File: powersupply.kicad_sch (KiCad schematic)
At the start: 25 parts, among them J1 5V In, J2 Vdrive In, U1 AP63203WU, U2 AP2112K-3.3

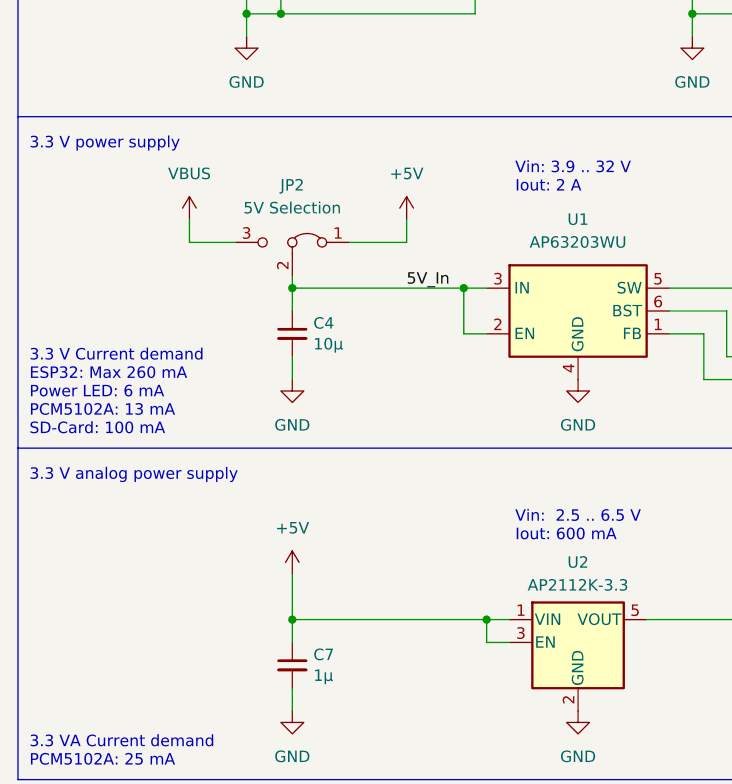
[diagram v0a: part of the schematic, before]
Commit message: - I2C entfernt - Logo hinzugefügt - Spannungsauswahl für Audio (USB oder +5V) hinzugefügt - Spannung für WS2812 LEDs ändert sich jetzt zusammen mit +5VD Auswahl
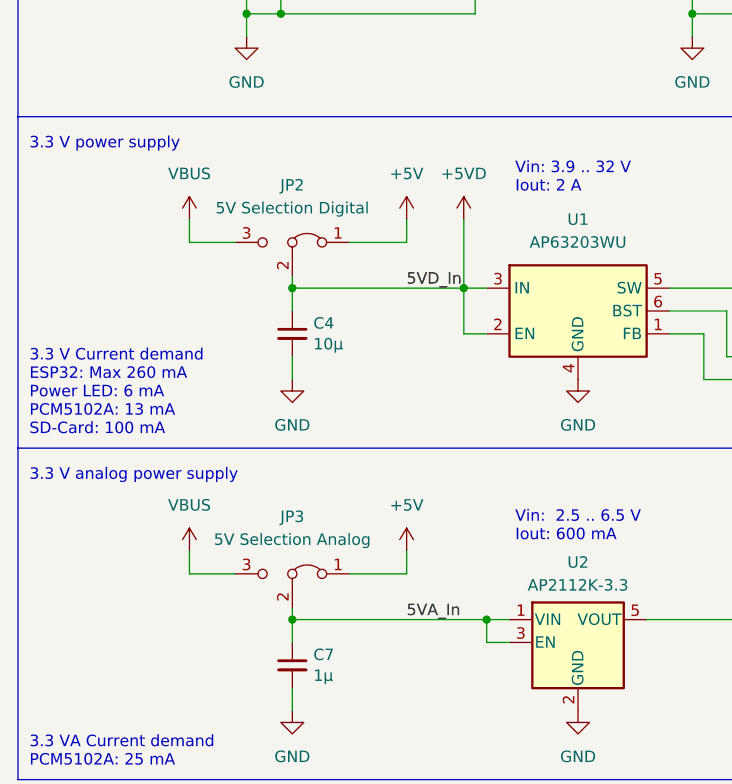
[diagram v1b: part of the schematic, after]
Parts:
- added JP3: 5V Selection Analog, Connector_PinHeader_2.54mm:PinHeader_1x03_P2.54mm_Vertical, symbol Jumper:Jumper_3_Bridged12
- JP2: value 5V Selection -> 5V Selection Digital
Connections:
- net +5V: now also JP3.1 (A); no longer C7.1, U2.1 (VIN), U2.3 (EN)
- net VBUS: now also JP3.3 (B)
- net 5V_In renamed +5VD
- new net 5VA_In: C7.1, JP3.2 (C), U2.1 (VIN), U2.3 (EN)

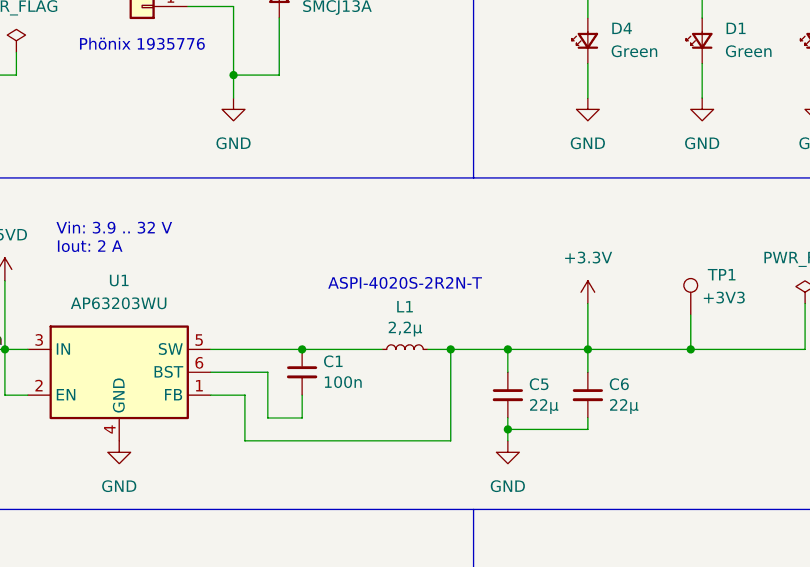
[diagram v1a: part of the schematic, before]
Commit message: Footprint changes
Changed WS2812 from 5050 to 2020
Changed ESP32 to correct revision
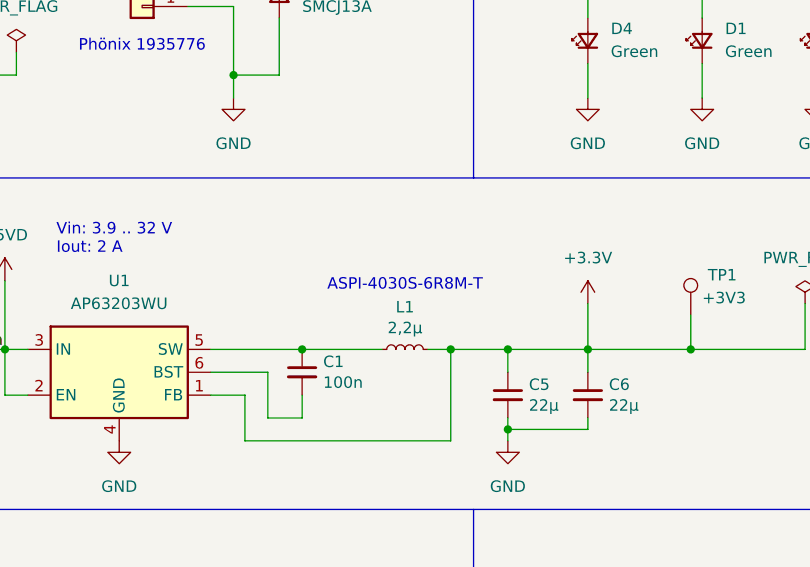
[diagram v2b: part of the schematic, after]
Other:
- note added: "ASPI-4030S-6R8M-T"
- note removed: "ASPI-4020S-2R2N-T"
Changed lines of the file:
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@@
 		)
 	)
-	(text "ASPI-4020S-2R2N-T"
+	(text "ASPI-4030S-6R8M-T"
 		(exclude_from_sim no)
 		(at 119.38 81.28 0)

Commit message: First Manufactured Version
A few silkscreen changes
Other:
- moved on the sheet: C1, U1
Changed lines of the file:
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@@
 	(text "Vin:  2.5 .. 6.5 V\nIout: 600 mA"
 		(exclude_from_sim no)
-		(at 80.645 112.395 0)
+		(at 85.344 110.236 0)
 		(effects
 			(font
@@
 	(text "Vin: 3.9 .. 32 V\nIout: 2 A"
 		(exclude_from_sim no)
-		(at 80.645 73.66 0)
+		(at 84.455 73.66 0)
 		(effects
 			(font
@@
 	)
 	(junction
+		(at 74.93 92.71)
+		(diameter 0)
+		(color 0 0 0 0)
+	)
+	(junction
 		(at 74.93 87.63)
 		(diameter 0)
@@
 	)
 	(junction
-		(at 107.95 87.63)
+		(at 111.76 87.63)
 		(diameter 0)
 		(color 0 0 0 0)
@@
 	(wire
 		(pts
-			(xy 97.79 87.63) (xy 107.95 87.63)
+			(xy 101.6 87.63) (xy 111.76 87.63)
 		)
 		(stroke
@@
 	(wire
 		(pts
-			(xy 77.47 92.71) (xy 74.93 92.71)
+			(xy 81.28 92.71) (xy 74.93 92.71)
 		)
 		(stroke
@@
 	(wire
 		(pts
-			(xy 97.79 92.71) (xy 101.6 92.71)
+			(xy 101.6 92.71) (xy 105.41 92.71)
 		)
 		(stroke
@@
 	(wire
 		(pts
-			(xy 97.79 90.17) (xy 104.14 90.17)
+			(xy 101.6 90.17) (xy 107.95 90.17)
 		)
 		(stroke
@@
 	(wire
 		(pts
-			(xy 107.95 95.25) (xy 107.95 92.71)
+			(xy 111.76 95.25) (xy 111.76 92.71)
 		)
 		(stroke
@@
 	(wire
 		(pts
-			(xy 104.14 90.17) (xy 104.14 95.25)
+			(xy 107.95 90.17) (xy 107.95 95.25)
 		)
 		(stroke
@@
 	(wire
 		(pts
-			(xy 74.93 87.63) (xy 77.47 87.63)
+			(xy 74.93 87.63) (xy 81.28 87.63)
 		)
 		(stroke
@@
 	(wire
 		(pts
-			(xy 104.14 95.25) (xy 107.95 95.25)
+			(xy 107.95 95.25) (xy 111.76 95.25)
 		)
 		(stroke
@@
 	(wire
 		(pts
+			(xy 77.47 119.38) (xy 77.47 124.46)
+		)
+		(stroke
+			(width 0)
+			(type default)
+		)
+	)
+	(wire
+		(pts
 			(xy 55.88 124.46) (xy 55.88 123.19)
 		)
@@
 	(wire
 		(pts
-			(xy 101.6 92.71) (xy 101.6 97.79)
+			(xy 105.41 92.71) (xy 105.41 97.79)
 		)
 		(stroke
@@
 	(wire
 		(pts
-			(xy 107.95 87.63) (xy 116.84 87.63)
+			(xy 111.76 87.63) (xy 116.84 87.63)
 		)
 		(stroke
@@
 	(wire
 		(pts
-			(xy 101.6 97.79) (xy 124.46 97.79)
+			(xy 105.41 97.79) (xy 124.46 97.79)
 		)
 		(stroke
@@
 		)
 	)
-	(label "5VD_In"
-		(at 68.58 87.63 0)
+	(label "+5VD"
+		(at 67.31 87.63 0)
 		(effects
 			(font
@@
 	(symbol
 		(lib_id "Device:C_Small")
-		(at 107.95 90.17 0)
+		(at 111.76 90.17 0)
 		(unit 1)
 		(exclude_from_sim no)
@@
 		(dnp no)
 		(property "Reference" "C1"
-			(at 110.2868 89.0016 0)
+			(at 114.0968 89.0016 0)
 			(effects
 				(font
@@
 		)
 		(property "Value" "100n"
-			(at 110.2868 91.313 0)
+			(at 114.0968 91.313 0)
 			(effects
 				(font
@@
 		)
 		(property "Footprint" "Capacitor_SMD:C_0603_1608Metric"
-			(at 107.95 90.17 0)
+			(at 111.76 90.17 0)
 			(effects
 				(font
@@
 		)
 		(property "Datasheet" "~"
-			(at 107.95 90.17 0)
+			(at 111.76 90.17 0)
 			(effects
 				(font
@@
 		)
 		(property "Description" ""
-			(at 107.95 90.17 0)
+			(at 111.76 90.17 0)
 			(effects
 				(font
@@
 	(symbol
 		(lib_id "Regulator_Switching:AP63203WU")
-		(at 87.63 90.17 0)
+		(at 91.44 90.17 0)
 		(unit 1)
 		(exclude_from_sim no)
@@
 		(fields_autoplaced yes)
 		(property "Reference" "U1"
-			(at 87.63 80.01 0)
+			(at 91.44 80.01 0)
 			(effects
 				(font
@@
 		)
 		(property "Value" "AP63203WU"
-			(at 87.63 82.55 0)
+			(at 91.44 82.55 0)
 			(effects
 				(font
@@
 		)
 		(property "Footprint" "Package_TO_SOT_SMD:TSOT-23-6"
-			(at 87.63 113.03 0)
+			(at 91.44 113.03 0)
 			(effects
 				(font
@@
 		)
 		(property "Datasheet" "https://www.diodes.com/assets/Datasheets/AP63200-AP63201-AP63203-AP63205.pdf"
-			(at 87.63 90.17 0)
+			(at 91.44 90.17 0)
 			(effects
 				(font
@@
 		)
 		(property "Description" ""
-			(at 87.63 90.17 0)
+			(at 91.44 90.17 0)
 			(effects
 				(font
@@
 	)
 	(symbol
+		(lib_id "power:PWR_FLAG")
+		(at 77.47 119.38 0)
+		(mirror y)
+		(unit 1)
+		(exclude_from_sim no)
+		(in_bom yes)
+		(on_board yes)
+		(dnp no)
+		(property "Reference" "#FLG08"
+			(at 77.47 117.475 0)
+			(effects
+				(font
+					(size 1.27 1.27)
+				)
+				(hide yes)
+			)
+		)
+		(property "Value" "PWR_FLAG"
+			(at 77.47 114.3 0)
+			(effects
+				(font
+					(size 1.27 1.27)
+				)
+			)
+		)
+		(property "Footprint" ""
+			(at 77.47 119.38 0)
+			(effects
+				(font
+					(size 1.27 1.27)
+				)
+				(hide yes)
+			)
+		)
+		(property "Datasheet" "~"
+			(at 77.47 119.38 0)
+			(effects
+				(font
+					(size 1.27 1.27)
+				)
+				(hide yes)
+			)
+		)
+		(property "Description" "Special symbol for telling ERC where power comes from"
+			(at 77.47 119.38 0)
+			(effects
+				(font
+					(size 1.27 1.27)
+				)
+				(hide yes)
+			)
+		)
+		(pin "1"
+		)
+		(instances
+			(project "BigCore"
+				(path "/9351c569-8a22-403a-823f-92ee14b5d151/de348b60-5b93-45ac-b286-4b82c099f6e0"
+					(reference "#FLG08")
+					(unit 1)
+				)
+			)
+		)
+	)
+	(symbol
 		(lib_id "Device:C_Small")
 		(at 55.88 92.71 0)
@@
 	)
 	(symbol
+		(lib_id "power:PWR_FLAG")
+		(at 74.93 92.71 0)
+		(mirror x)
+		(unit 1)
+		(exclude_from_sim no)
+		(in_bom yes)
+		(on_board yes)
+		(dnp no)
+		(property "Reference" "#FLG07"
+			(at 74.93 94.615 0)
+			(effects
+				(font
+					(size 1.27 1.27)
+				)
+				(hide yes)
+			)
+		)
+		(property "Value" "PWR_FLAG"
+			(at 74.93 97.79 0)
+			(effects
+				(font
+					(size 1.27 1.27)
+				)
+			)
+		)
+		(property "Footprint" ""
+			(at 74.93 92.71 0)
+			(effects
+				(font
+					(size 1.27 1.27)
+				)
+				(hide yes)
+			)
+		)
+		(property "Datasheet" "~"
+			(at 74.93 92.71 0)
+			(effects
+				(font
+					(size 1.27 1.27)
+				)
+				(hide yes)
+			)
+		)
+		(property "Description" "Special symbol for telling ERC where power comes from"
+			(at 74.93 92.71 0)
+			(effects
+				(font
+					(size 1.27 1.27)
+				)
+				(hide yes)
+			)
+		)
+		(pin "1"
+		)
+		(instances
+			(project "BigCore"
+				(path "/9351c569-8a22-403a-823f-92ee14b5d151/de348b60-5b93-45ac-b286-4b82c099f6e0"
+					(reference "#FLG07")
+					(unit 1)
+				)
+			)
+		)
+	)
+	(symbol
 		(lib_id "Device:C_Polarized_Small")
 		(at 190.5 87.63 0)
@@
 		(lib_name "GND_1")
 		(lib_id "power:GND")
-		(at 87.63 97.79 0)
+		(at 91.44 97.79 0)
 		(unit 1)
 		(exclude_from_sim no)
@@
 		(fields_autoplaced yes)
 		(property "Reference" "#PWR017"
-			(at 87.63 104.14 0)
+			(at 91.44 104.14 0)
 			(effects
 				(font
@@
 		)
 		(property "Value" "GND"
-			(at 87.63 102.87 0)
+			(at 91.44 102.87 0)
 			(effects
 				(font
@@
 		)
 		(property "Footprint" ""
-			(at 87.63 97.79 0)
+			(at 91.44 97.79 0)
 			(effects
 				(font
@@
 		)
 		(property "Datasheet" ""
-			(at 87.63 97.79 0)
+			(at 91.44 97.79 0)
 			(effects
 				(font
@@
 		)
 		(property "Description" "Power symbol creates a global label with name \"GND\" , ground"
-			(at 87.63 97.79 0)
+			(at 91.44 97.79 0)
 			(effects
 				(font
